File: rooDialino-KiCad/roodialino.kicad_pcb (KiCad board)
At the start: 2 copper layers, 65 x 30 mm, 62 parts, among them J1 Raspi Connector, J2 ICSP, J3 FTDI, J4 IR Receiver, J5 IR LED, Q1 2N7002, Q2 2N7002, Q3 2N7002, SW1 SW_Push, U1 ATmega328P, U2 TSOP312xx, U3 TXS0108EPW, Y1 16MHz

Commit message: More routing
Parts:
- moved TP1 69.8 mm to (142.1, 126.3)
- moved TP8 52.7 mm to (147.2, 87.2)
- moved TP2 51.8 mm to (149.5, 126.8)
- moved TP4 49.5 mm to (164.0, 84.9)
- moved TP3 48.0 mm to (158.4, 85.2)
- moved TP5 34.8 mm to (136.0, 125.6)
- moved TP6 28.5 mm to (154.3, 124.8)
- moved J2 26.3 mm to (172.6, 102.2)
- moved R6 24.0 mm to (148.5, 113.9)
- moved R5 22.6 mm to (152.5, 113.9)
- moved R2 14.6 mm to (156.6, 106.8), turned to 180 degrees
- moved C7 13.5 mm to (150.2, 100.9)
- moved R7 12.7 mm to (137.8, 117.2), turned to 180 degrees
- moved C2 12.6 mm to (154.8, 100.9)
- moved C8 12.5 mm to (145.9, 100.9)
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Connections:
- U3 pad 1: /VOL+3 -> /RST3
- U3 pad 12: /~RST~ -> /TX5
- U3 pad 13: /SCK5 -> /RX5
- U3 pad 14: /MOSI5 -> /VOL+5
- U3 pad 16: /RX5 -> /VOL-5
- U3 pad 17: /TX5 -> /MOSI5
- U3 pad 18: /VOL-5 -> /SCK5
- U3 pad 20: /VOL+5 -> /~RST~
- U3 pad 3: /VOL-3 -> /SCK3
- U3 pad 4: /RX3 -> /MOSI3
- U3 pad 5: /TX3 -> /VOL-3
- U3 pad 7: /MOSI3 -> /VOL+3
- U3 pad 8: /SCK3 -> /RX3
- U3 pad 9: /RST3 -> /TX3
- Y1 pad 1: Net-(C4-Pad2) -> Net-(C5-Pad1)
- Y1 pad 2: Net-(C5-Pad1) -> Net-(C4-Pad2)
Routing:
- net /SCK5: track 0.00 -> 61.0 mm, vias 0 -> 4
- net Net-(D6-Pad1): track 0.00 -> 41.5 mm, vias 0 -> 2
- net /IRRCV: track 0.00 -> 39.3 mm, vias 0 -> 3
- net /RST3: track 0.00 -> 39.1 mm
- net +5V: track 0.00 -> 35.4 mm, vias 0 -> 6
- net +3V3: track 0.00 -> 34.5 mm
- net /BTTN: track 0.00 -> 33.1 mm, vias 0 -> 2
- net /MISO5: track 0.00 -> 25.3 mm, vias 0 -> 4
- net /A0: track 0.00 -> 24.8 mm, vias 0 -> 4
- net /SCK3: track 0.00 -> 22.5 mm, vias 0 -> 1
- net /MISO3: track 0.00 -> 21.7 mm, vias 0 -> 1
- net /LEDVOL-: track 0.00 -> 21.3 mm
- net /VOL-3: track 0.00 -> 19.7 mm, vias 0 -> 1
- net /MOSI3: track 0.00 -> 18.6 mm
- net /D9: track 0.00 -> 18.3 mm, vias 0 -> 2
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- added copper zone on B.Cu, net +5V
- added copper zone on F.Cu, net GNDD
- removed copper zone on B.Cu, net GND
- removed copper zone on F.Cu, net GND
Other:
- board text added: "Learn: Off"
- board text added: "Learn: On"
- board text added: "Relay"
- board text added: "Vol+"
- board text added: "Vol-"
- board text added: "rooDial IR Relay • Rev. A"

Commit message: Nets complete!
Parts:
- moved TP2 16.1 mm to (133.5, 128.1)
- moved TP5 1.82 mm to (137.7, 124.8)
- moved TP1 0.77 mm to (141.4, 126.2)
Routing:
- net Net-(D8-Pad1): track 0.00 -> 64.8 mm, vias 0 -> 6
- net /TX5: track 16.0 -> 71.8 mm, vias 0 -> 5
- net /RX5: track 15.8 -> 71.1 mm, vias 2 -> 6
- net /GPIO5: track 0.00 -> 55.0 mm, vias 0 -> 1
- net /GPIO6: track 0.00 -> 54.3 mm, vias 0 -> 2
- net /~RST~: track 13.2 -> 64.7 mm, vias 2 -> 8
- net /MOSI5: track 18.0 -> 66.3 mm, vias 2 -> 9
- net /MISO5: track 25.3 -> 64.4 mm, vias 4 -> 7
- net Net-(Q1-Pad1): track 0.00 -> 34.9 mm, vias 0 -> 2
- net Net-(D7-Pad1): track 0.00 -> 27.1 mm, vias 0 -> 4
- net Net-(C6-Pad1): track 0.00 -> 24.1 mm, vias 0 -> 4
- net +5V: track 35.4 -> 56.8 mm, vias 6 -> 9
- net +3V3: track 34.5 -> 54.8 mm, vias 0 -> 2
- net Net-(D5-Pad2): track 0.00 -> 20.1 mm, vias 0 -> 2
- net Net-(D3-Pad2): track 0.00 -> 15.0 mm
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
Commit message: Looking good, that PCB
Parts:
- removed TP1: D9, TestPoint:TestPoint_THTPad_D1.5mm_Drill0.7mm
- removed TP2: A0, TestPoint:TestPoint_THTPad_D1.5mm_Drill0.7mm
- removed TP3: GPIO5, TestPoint:TestPoint_THTPad_D1.5mm_Drill0.7mm
- removed TP4: GPIO6, TestPoint:TestPoint_THTPad_D1.5mm_Drill0.7mm
- removed TP5: IRTX, TestPoint:TestPoint_THTPad_D1.5mm_Drill0.7mm
- removed TP6: IRRCV, TestPoint:TestPoint_THTPad_D1.5mm_Drill0.7mm
- removed TP7: GND, TestPoint:TestPoint_THTPad_D1.5mm_Drill0.7mm
- removed TP8: +3.3V, TestPoint:TestPoint_THTPad_D1.5mm_Drill0.7mm
- removed TP9: +5V, TestPoint:TestPoint_THTPad_D1.5mm_Drill0.7mm
- D7: footprint LED_THT:LED_D5.0mm_Clear -> LED_THT:LED_D5.0mm_IRBlack
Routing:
- net +5V: track 56.8 -> 58.0 mm
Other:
- board text added: "by Friedemann Wachsmuth 2021 • Rev. A"
- board text added: "rooDial IR Relay"
- board text removed: "rooDial IR Relay • Rev. A"

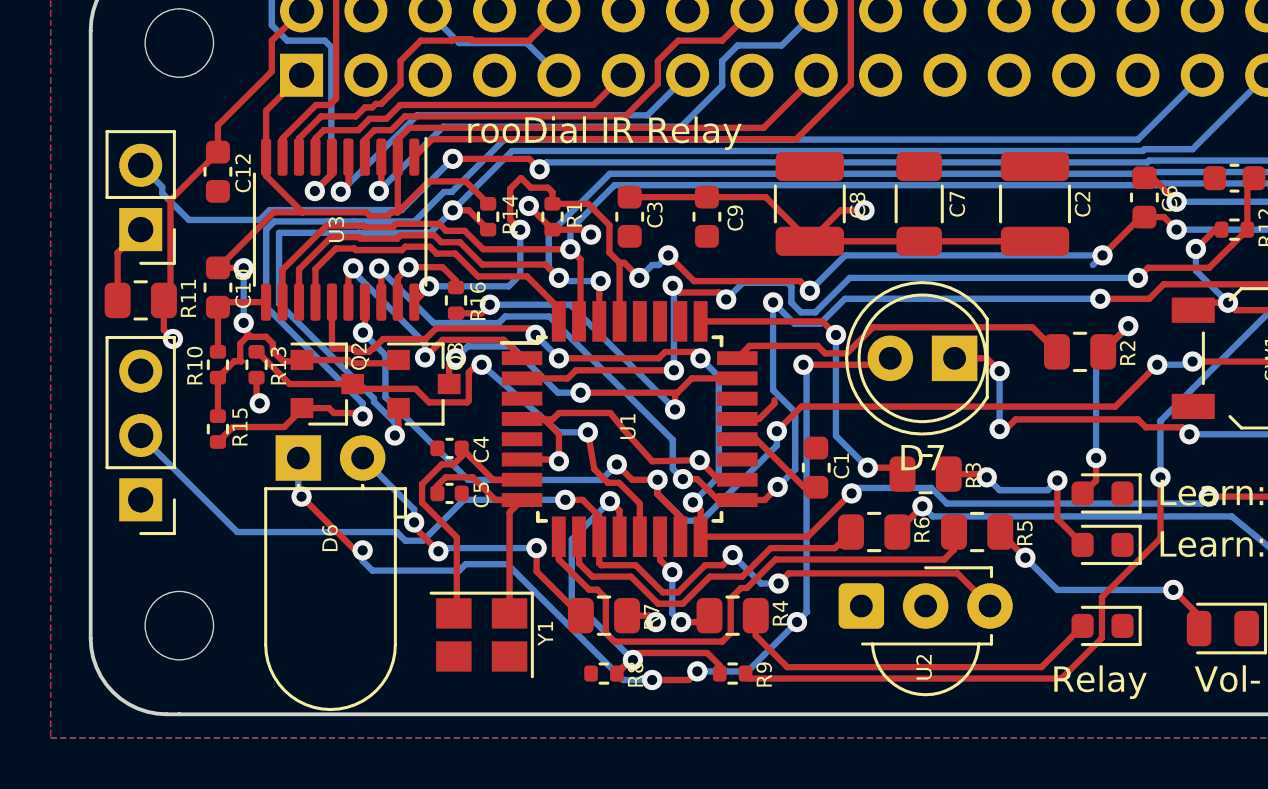
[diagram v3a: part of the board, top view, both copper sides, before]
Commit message: Fixing the crystal footprint
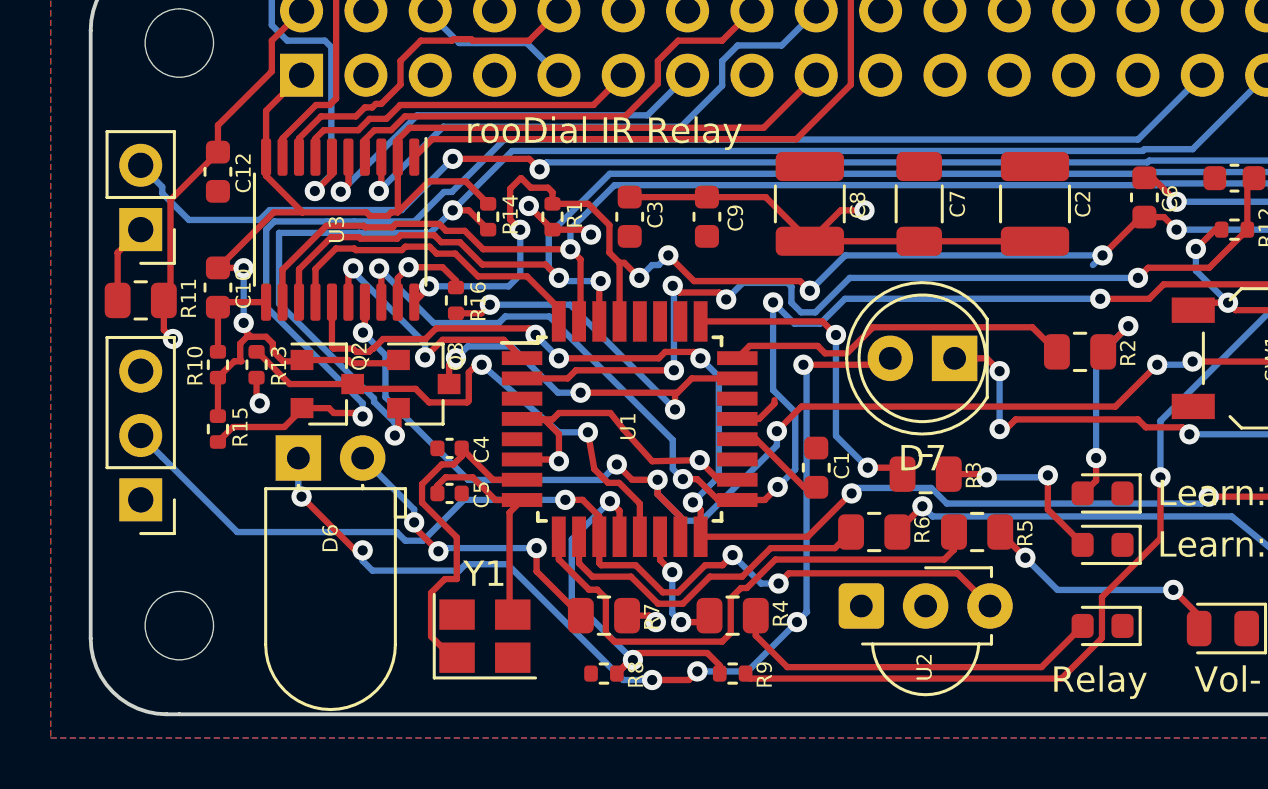
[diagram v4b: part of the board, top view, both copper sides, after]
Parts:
- Y1: value 16MHz -> 16 MHz
- moved Y1 0.13 mm to (133.1, 118.0), turned to 0 degrees
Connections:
- Y1 pad 1: Net-(C5-Pad1) -> Net-(C4-Pad2)
- Y1 pad 2: Net-(C4-Pad2) -> GNDD
- Y1 pad 3: (no net) -> Net-(C5-Pad1)
- Y1 pad 4: (no net) -> GNDD
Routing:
- net Net-(C4-Pad2): track 10.9 -> 13.6 mm
